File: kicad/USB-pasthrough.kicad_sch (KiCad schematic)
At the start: 96 parts, among them J1 USB_Power, J10 MicroSD, J2 USB_C, J3 Power_Sel, J4 Cortex Debug, J5 SPI Display, J6 SWD, J7 Serial, J8 USB_A, J9 SD-1-A, SW1 Boot0, SW2 Reset, U1 AMS1117, U2 STM32F723VET6, Y1 8 MHz

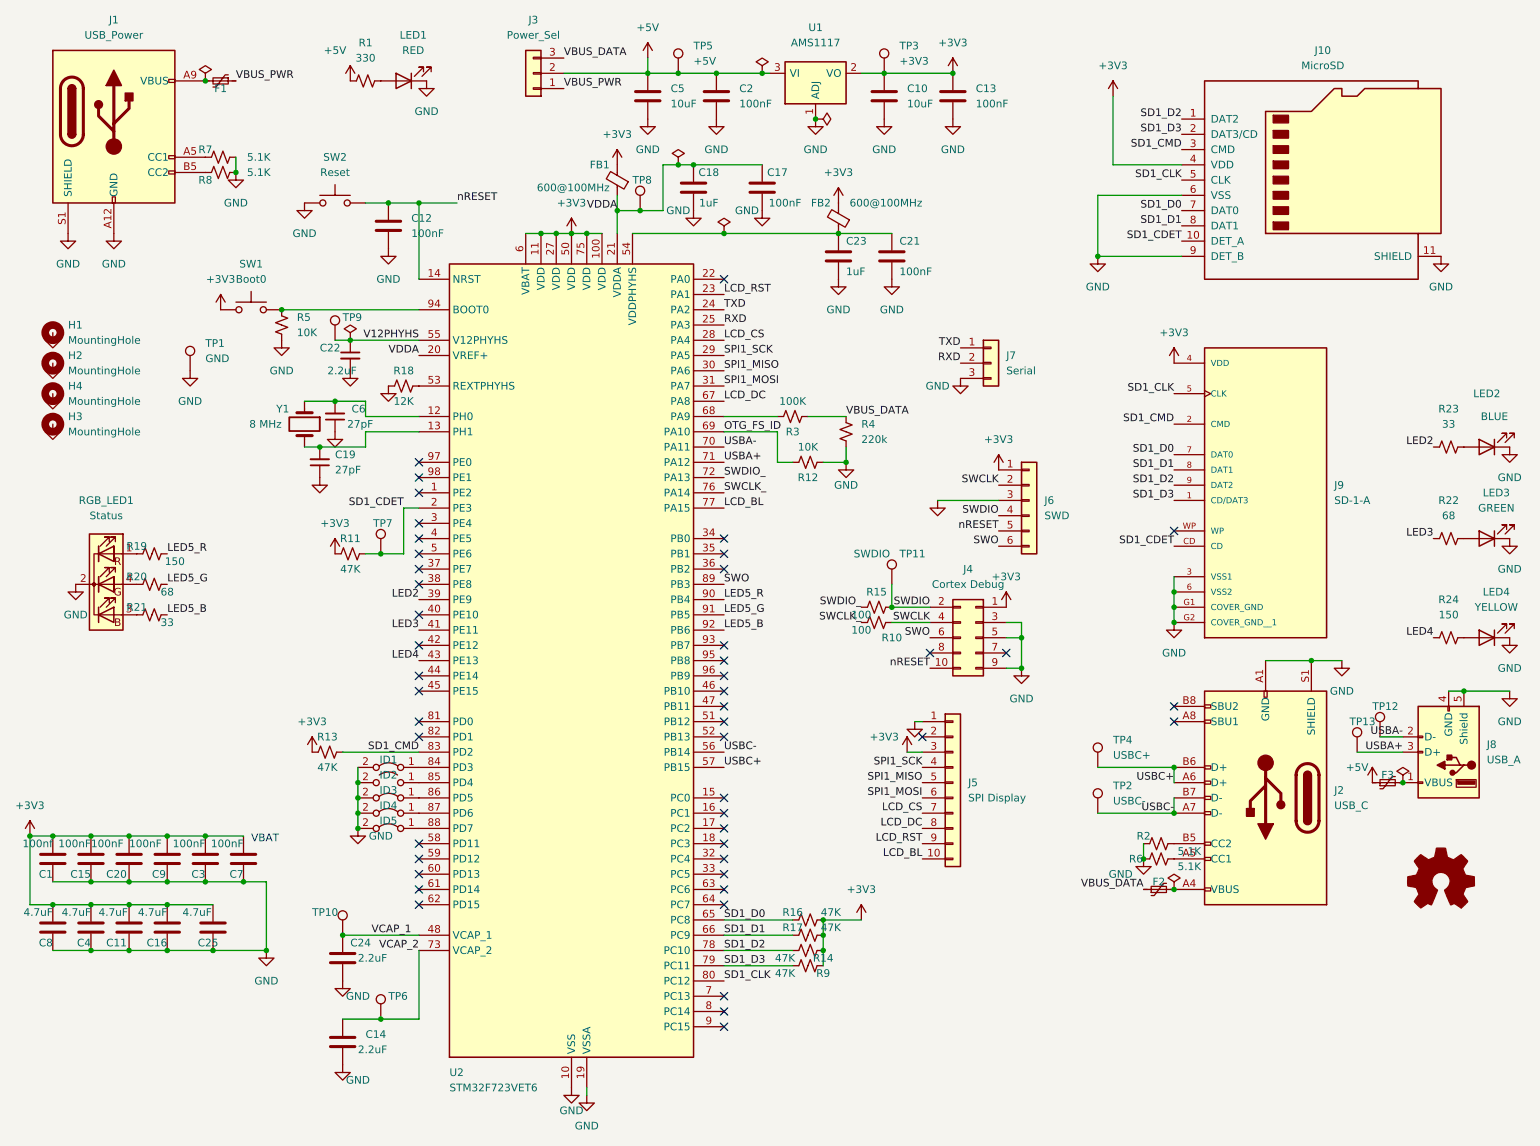
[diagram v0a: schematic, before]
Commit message: Schematic: add TPS2065C USB-A VBUS switch, remove PA9 VBUS divider
- Add TPS2065C (via TPS2041B symbol) on USB-A VBUS: IN=5V, OUT=USBA_VBUS,
  EN=PB0 (active-high, GPIO-low at reset keeps VBUS off)
- Remove VBUS_DATA voltage divider on PA9 (no longer needed)

Co-Authored-By: Claude Sonnet 4.6 <noreply@anthropic.com>
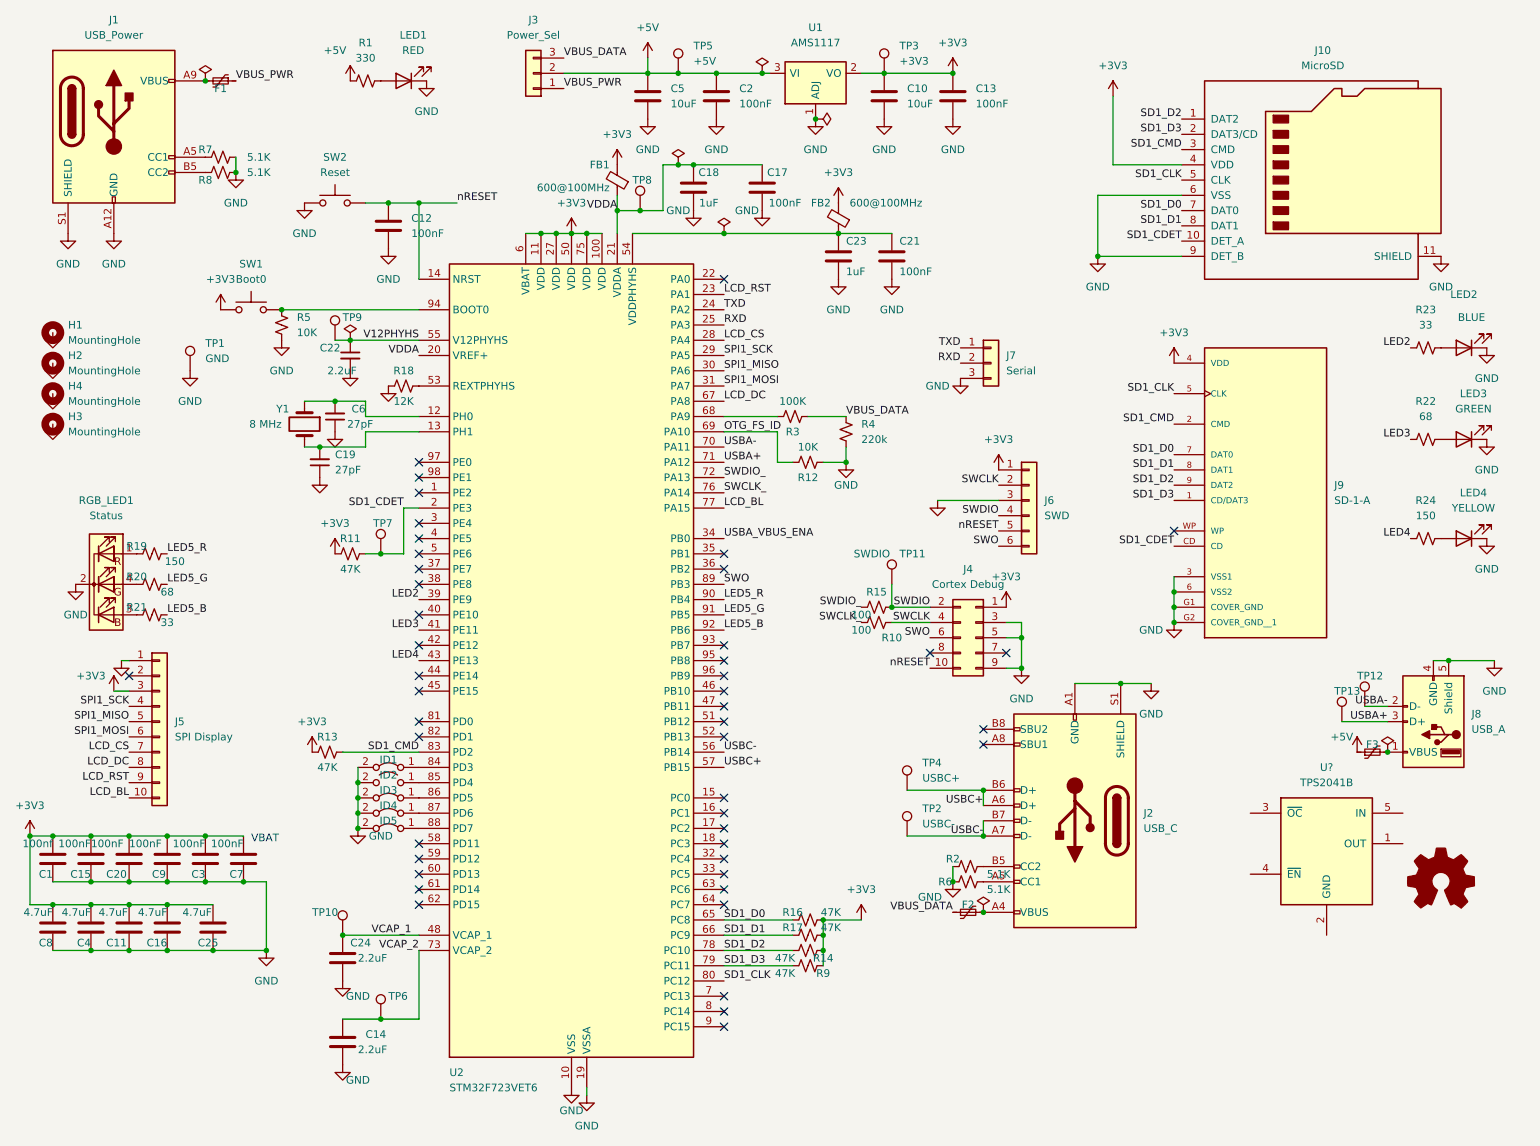
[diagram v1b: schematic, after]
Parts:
- added U?: TPS2041B, Package_TO_SOT_SMD:SOT-23-5, symbol Power_Management:TPS2041B
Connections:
- net USBA_VBUS_ENA: now reaches U2.34 (PB0)
- no-connect marks 47 -> 46
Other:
- moved on the sheet: F2, F3, J2, J5, J8, LED2, LED3, LED4, R2, R22, R23, R24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
